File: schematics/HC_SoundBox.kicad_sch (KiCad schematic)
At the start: 12 parts, among them SW1 SW_Push, SW2 SW_Push, SW3 SW_Push, U1 ESP32 DEVKITC V4 WROOM-32U, U2 MAX98357A, U3 SPI MicroSD Reader, U4 KY-040

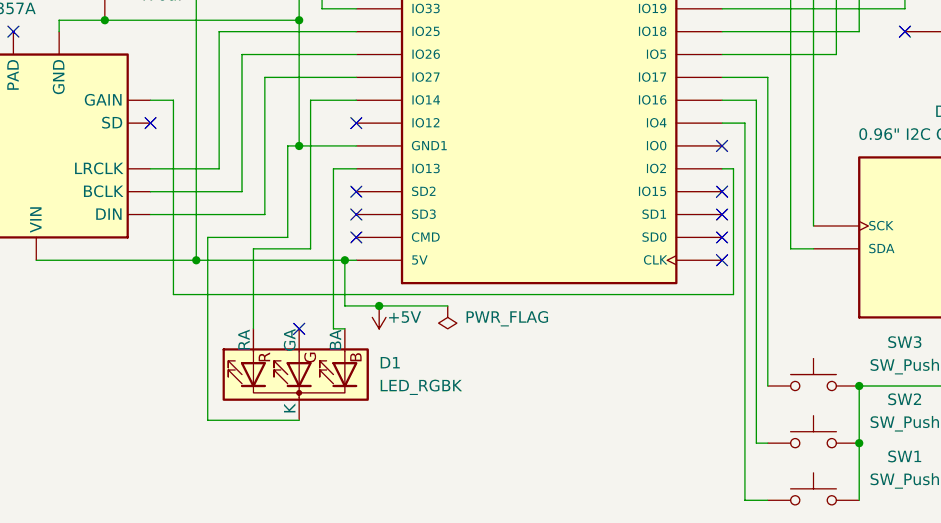
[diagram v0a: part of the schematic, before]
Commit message: new feature: added rgb led that changes color based on where the user navigates to
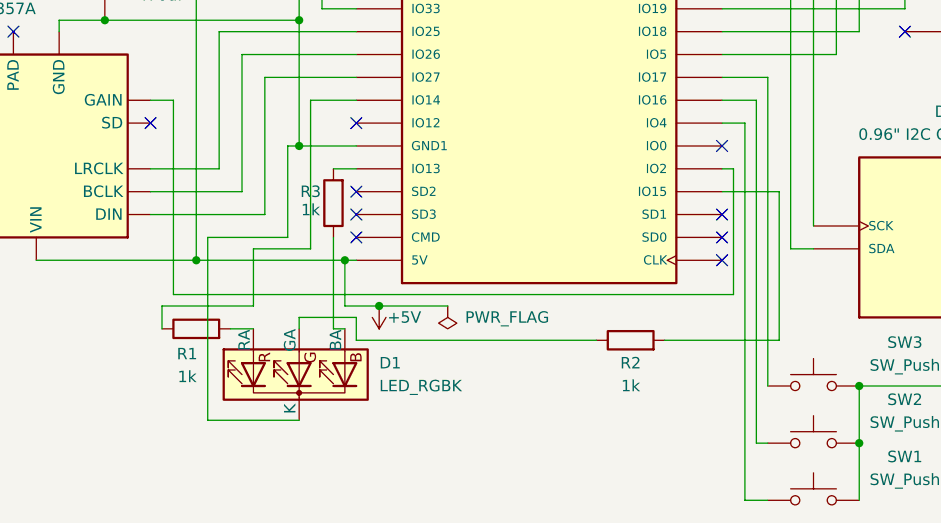
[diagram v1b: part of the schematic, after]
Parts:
- added R1, R2, R3: 1k, symbol Device:R
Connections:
- net at U1.12 (IO14): now also R1.1; no longer D1.1 (RA)
- net at D1.3 (BA): now also R3.1; no longer U1.15 (IO13)
- net at U1.23 (IO15): now also R2.2
- net at D1.2 (GA): now also R2.1
- new net: R3.2, U1.15 (IO13)
- new net: D1.1 (RA), R1.2
- no-connect marks 21 -> 19

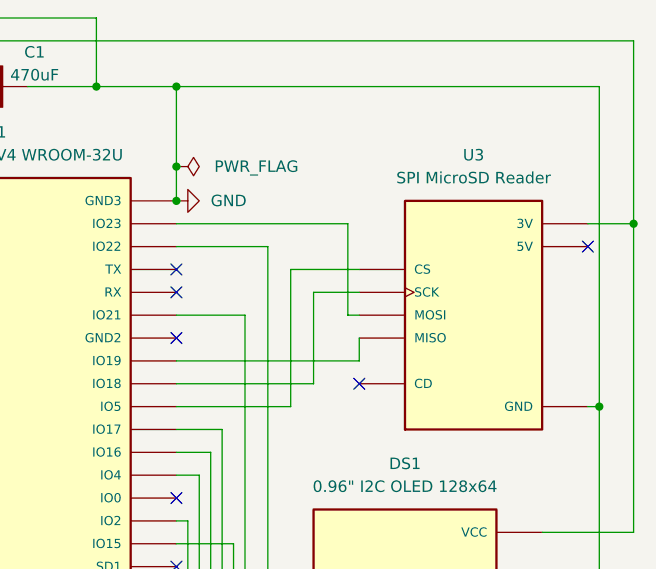
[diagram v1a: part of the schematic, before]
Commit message: bug fix: add a capacitor across the power and gnd of the sd module to reduce failures in reading
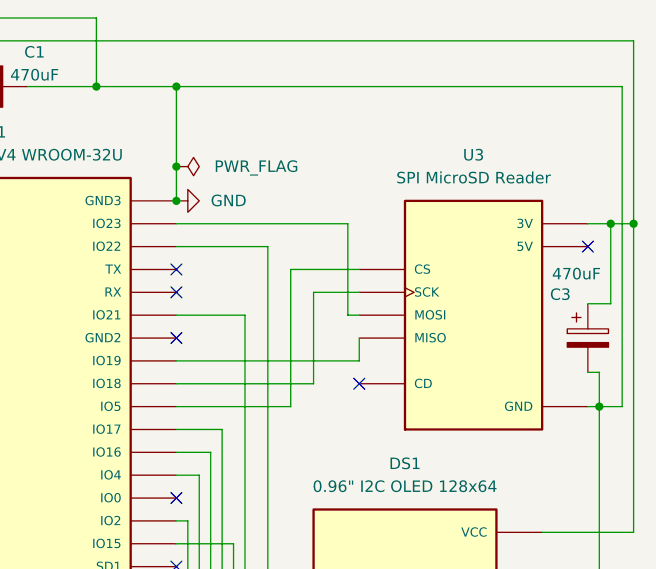
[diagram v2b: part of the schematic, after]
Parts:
- added C3: 470uF, symbol Device:C_Polarized
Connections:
- net GND: now also C3.2
- net at C1.1, DS1.1 (VCC), U1.1 (3V3)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: now also C3.1
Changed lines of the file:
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@@
 	)
 	(junction
-		(at 205.74 95.25)
-		(diameter 0)
-		(color 0 0 0 1)
-	)
-	(junction
 		(at 90.17 91.44)
 		(diameter 0)
@@
 	)
 	(junction
+		(at 207.01 74.93)
+		(diameter 0)
+		(color 255 0 0 1)
+	)
+	(junction
 		(at 100.33 118.11)
 		(diameter 0)
@@
 	)
 	(junction
+		(at 205.74 95.25)
+		(diameter 0)
+		(color 0 0 0 1)
+	)
+	(junction
 		(at 111.76 105.41)
 		(diameter 0)
@@
 	(wire
 		(pts
-			(xy 177.8 74.93) (xy 158.75 74.93)
+			(xy 208.28 95.25) (xy 205.74 95.25)
 		)
 		(stroke
 			(width 0)
 			(type default)
-			(color 255 0 255 1)
+			(color 0 0 0 1)
 		)
 	)
 	(wire
 		(pts
-			(xy 111.76 68.58) (xy 111.76 52.07)
+			(xy 177.8 74.93) (xy 158.75 74.93)
 		)
 		(stroke
 			(width 0)
 			(type default)
-			(color 0 0 0 1)
+			(color 255 0 255 1)
 		)
 	)
 	(wire
 		(pts
-			(xy 158.75 110.49) (xy 165.1 110.49)
+			(xy 111.76 68.58) (xy 111.76 52.07)
 		)
 		(stroke
 			(width 0)
 			(type default)
+			(color 0 0 0 1)
 		)
 	)
 	(wire
 		(pts
-			(xy 205.74 59.69) (xy 205.74 95.25)
+			(xy 158.75 110.49) (xy 165.1 110.49)
 		)
 		(stroke
 			(width 0)
 			(type default)
-			(color 0 0 0 1)
 		)
 	)
@@
 	(wire
 		(pts
+			(xy 205.74 91.44) (xy 205.74 95.25)
+		)
+		(stroke
+			(width 0)
+			(type default)
+			(color 0 0 0 1)
+		)
+	)
+	(wire
+		(pts
 			(xy 171.45 80.01) (xy 171.45 95.25)
 		)
@@
 	(wire
 		(pts
+			(xy 207.01 83.82) (xy 207.01 74.93)
+		)
+		(stroke
+			(width 0)
+			(type default)
+			(color 255 0 0 1)
+		)
+	)
+	(wire
+		(pts
 			(xy 163.83 132.08) (xy 163.83 97.79)
 		)
@@
 	(wire
 		(pts
+			(xy 204.47 83.82) (xy 207.01 83.82)
+		)
+		(stroke
+			(width 0)
+			(type default)
+			(color 255 0 0 1)
+		)
+	)
+	(wire
+		(pts
+			(xy 204.47 91.44) (xy 205.74 91.44)
+		)
+		(stroke
+			(width 0)
+			(type default)
+			(color 0 0 0 1)
+		)
+	)
+	(wire
+		(pts
 			(xy 116.84 118.11) (xy 118.11 118.11)
 		)
@@
 	(wire
 		(pts
+			(xy 207.01 74.93) (xy 209.55 74.93)
+		)
+		(stroke
+			(width 0)
+			(type default)
+			(color 255 0 0 1)
+		)
+	)
+	(wire
+		(pts
 			(xy 205.74 132.08) (xy 205.74 121.92)
 		)
@@
 	(wire
 		(pts
-			(xy 204.47 74.93) (xy 209.55 74.93)
+			(xy 204.47 74.93) (xy 207.01 74.93)
 		)
 		(stroke
@@
 	(wire
 		(pts
-			(xy 158.75 59.69) (xy 205.74 59.69)
+			(xy 158.75 59.69) (xy 208.28 59.69)
 		)
 		(stroke
@@
 	(wire
 		(pts
+			(xy 208.28 59.69) (xy 208.28 95.25)
+		)
+		(stroke
+			(width 0)
+			(type default)
+			(color 0 0 0 1)
+		)
+	)
+	(wire
+		(pts
 			(xy 113.03 116.84) (xy 113.03 100.33)
 		)
@@
 					(unit 1)
 				)
+			)
+		)
+	)
+	(symbol
+		(lib_id "Device:C_Polarized")
+		(at 204.47 87.63 0)
+		(unit 1)
+		(body_style 1)
+		(exclude_from_sim no)
+		(in_bom yes)
+		(on_board yes)
+		(in_pos_files yes)
+		(dnp no)
+		(property "Reference" "C3"
+			(at 201.422 82.804 0)
+			(show_name no)
+			(do_not_autoplace no)
+			(effects
+				(font
+					(size 1.27 1.27)
+				)
+			)
+		)
+		(property "Value" "470uF"
+			(at 203.2 80.518 0)
+			(show_name no)
+			(do_not_autoplace no)
+			(effects
+				(font
+					(size 1.27 1.27)
+				)
+			)
+		)
+		(property "Footprint" ""
+			(at 205.4352 91.44 0)
+			(hide yes)
+			(show_name no)
+			(do_not_autoplace no)
+			(effects
+				(font
+					(size 1.27 1.27)
+				)
+			)
+		)
+		(property "Datasheet" ""
+			(at 204.47 87.63 0)
+			(hide yes)
+			(show_name no)
+			(do_not_autoplace no)
+			(effects
+				(font
+					(size 1.27 1.27)
+				)
+			)
+		)
+		(property "Description" "Polarized capacitor"
+			(at 204.47 87.63 0)
+			(hide yes)
+			(show_name no)
+			(do_not_autoplace no)
+			(effects
+				(font
+					(size 1.27 1.27)
+				)
+			)
+		)
+		(pin "1"
+		)
+		(pin "2"
+		)
+		(instances
+			(project "HC_SoundBox"
+				(path "/8affcf08-7ea6-4c06-a2bd-de2bfdf79792"
+					(reference "C3")
+					(unit 1)
+				)

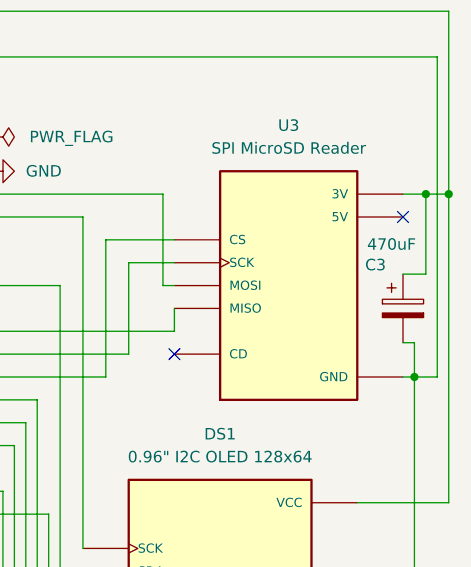
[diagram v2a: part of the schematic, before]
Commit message: bug fix: remove capacitor across power of sd module because it does not actually help and makes the card fail more often
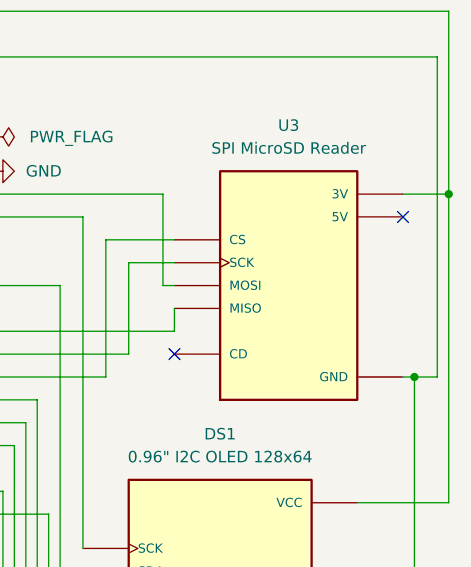
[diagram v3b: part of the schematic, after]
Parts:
- removed C3: 470uF, symbol Device:C_Polarized
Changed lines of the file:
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@@
 	)
 	(junction
-		(at 207.01 74.93)
-		(diameter 0)
-		(color 255 0 0 1)
-	)
-	(junction
 		(at 100.33 118.11)
 		(diameter 0)
@@
 	(wire
 		(pts
-			(xy 205.74 91.44) (xy 205.74 95.25)
-		)
-		(stroke
-			(width 0)
-			(type default)
-			(color 0 0 0 1)
-		)
-	)
-	(wire
-		(pts
 			(xy 171.45 80.01) (xy 171.45 95.25)
 		)
@@
 	(wire
 		(pts
-			(xy 207.01 83.82) (xy 207.01 74.93)
-		)
-		(stroke
-			(width 0)
-			(type default)
-			(color 255 0 0 1)
-		)
-	)
-	(wire
-		(pts
 			(xy 163.83 132.08) (xy 163.83 97.79)
 		)
@@
 	(wire
 		(pts
-			(xy 204.47 83.82) (xy 207.01 83.82)
-		)
-		(stroke
-			(width 0)
-			(type default)
-			(color 255 0 0 1)
-		)
-	)
-	(wire
-		(pts
-			(xy 204.47 91.44) (xy 205.74 91.44)
-		)
-		(stroke
-			(width 0)
-			(type default)
-			(color 0 0 0 1)
-		)
-	)
-	(wire
-		(pts
 			(xy 116.84 118.11) (xy 118.11 118.11)
 		)
@@
 	(wire
 		(pts
-			(xy 207.01 74.93) (xy 209.55 74.93)
-		)
-		(stroke
-			(width 0)
-			(type default)
-			(color 255 0 0 1)
-		)
-	)
-	(wire
-		(pts
 			(xy 205.74 132.08) (xy 205.74 121.92)
 		)
@@
 	(wire
 		(pts
-			(xy 204.47 74.93) (xy 207.01 74.93)
+			(xy 204.47 74.93) (xy 209.55 74.93)
 		)
 		(stroke
@@
 					(unit 1)
 				)
-			)
-		)
-	)
-	(symbol
-		(lib_id "Device:C_Polarized")
-		(at 204.47 87.63 0)
-		(unit 1)
-		(body_style 1)
-		(exclude_from_sim no)
-		(in_bom yes)
-		(on_board yes)
-		(in_pos_files yes)
-		(dnp no)
-		(property "Reference" "C3"
-			(at 201.422 82.804 0)
-			(show_name no)
-			(do_not_autoplace no)
-			(effects
-				(font
-					(size 1.27 1.27)
-				)
-			)
-		)
-		(property "Value" "470uF"
-			(at 203.2 80.518 0)
-			(show_name no)
-			(do_not_autoplace no)
-			(effects
-				(font
-					(size 1.27 1.27)
-				)
-			)
-		)
-		(property "Footprint" ""
-			(at 205.4352 91.44 0)
-			(hide yes)
-			(show_name no)
-			(do_not_autoplace no)
-			(effects
-				(font
-					(size 1.27 1.27)
-				)
-			)
-		)
-		(property "Datasheet" ""
-			(at 204.47 87.63 0)
-			(hide yes)
-			(show_name no)
-			(do_not_autoplace no)
-			(effects
-				(font
-					(size 1.27 1.27)
-				)
-			)
-		)
-		(property "Description" "Polarized capacitor"
-			(at 204.47 87.63 0)
-			(hide yes)
-			(show_name no)
-			(do_not_autoplace no)
-			(effects
-				(font
-					(size 1.27 1.27)
-				)
-			)
-		)
-		(pin "1"
-		)
-		(pin "2"
-		)
-		(instances
-			(project "HC_SoundBox"
-				(path "/8affcf08-7ea6-4c06-a2bd-de2bfdf79792"
-					(reference "C3")
-					(unit 1)
-				)

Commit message: perf: add 0.1uf ceramic capacitors across power of multiple components for better performance and reliability
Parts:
- removed SW2, SW3: SW_Push, symbol Switch:SW_Push
- added C3, C4, C5, C6: 0.1uF, symbol Device:C
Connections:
- net +5V: now also C6.1
- net GND: now also C3.1, C4.2, C5.2, C6.2
- net at C1.1, DS1.1 (VCC), U1.1 (3V3)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: now also C3.2, C4.1, C5.1
- no-connect marks 19 -> 21
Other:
- moved on the sheet: SW1
